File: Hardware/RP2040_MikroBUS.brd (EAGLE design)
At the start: 30.5 x 94 mm, 144 parts, among them J1 SWD, J3 Qwiic, J5 USB C, J6 microSD, Q1 20V/4.2A/52mΩ/1.4W, U2 MAX17048, U3 MCP73831, U4 W25QXX128MBIT, U5 RP2040, U6 WS2812-2020, U7 3.3V, Y2 12MHz

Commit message: Add raspi logos to repo
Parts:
- removed U$17: (no value), output:#I�C#0
- added U$72: (no value), output:#I2C#0
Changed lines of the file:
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@@
 <?xml version="1.0" encoding="utf-8"?>
 <!DOCTYPE eagle SYSTEM "eagle.dtd">
-<eagle version="9.5.2">
+<eagle version="9.4.2">
 <drawing>
 <settings>
-<setting alwaysvectorfont="no"/>
+<setting alwaysvectorfont="yes"/>
 <setting keepoldvectorfont="yes"/>
 <setting verticaltext="up"/>
@@
 <layer number="95" name="Names" color="7" fill="1" visible="no" active="no"/>
 <layer number="96" name="Values" color="7" fill="1" visible="no" active="no"/>
-<layer number="2" name="gndvert" color="10" fill="7" visible="yes" active="yes"/>
-<layer number="15" name="pwrhorz" color="4" fill="7" visible="yes" active="yes"/>
+<layer number="2" name="gndvert" color="10" fill="7" visible="no" active="yes"/>
+<layer number="15" name="pwrhorz" color="4" fill="7" visible="no" active="yes"/>
 <layer number="3" name="Route3" color="4" fill="3" visible="no" active="no"/>
 <layer number="4" name="Route4" color="1" fill="4" visible="no" active="no"/>
@@
 </polygon>
 <text x="13.081" y="-19.177" size="1.778" layer="51" font="vector" ratio="15">N. Poole</text>
-<polygon width="0.2032" layer="22">
-<vertex x="12.0396" y="11.2522"/>
-<vertex x="10.033" y="11.2522"/>
-<vertex x="10.033" y="10.5156"/>
-<vertex x="11.049" y="10.5156"/>
-<vertex x="11.049" y="11.2268"/>
-<vertex x="11.4046" y="11.2268"/>
-</polygon>
-<polygon width="0.2032" layer="22">
-<vertex x="11.811" y="7.7978"/>
-<vertex x="10.033" y="7.7978"/>
-<vertex x="10.033" y="8.5598"/>
-<vertex x="11.049" y="8.5598"/>
-<vertex x="11.049" y="7.7978"/>
-</polygon>
 <text x="48.26" y="45.72" size="1.778" layer="51" font="vector" ratio="15">Four Layer</text>
 <text x="48.26" y="43.18" size="1.778" layer="51" font="vector" ratio="15">1.6mm FR4</text>
@@
 </element>
 <element name="U$16" library="output" package="PWR0" value="" x="22.86" y="5.08" smashed="yes"/>
-<element name="U$17" library="output" package="#I�C#0" value="" x="10.4394" y="9.525" smashed="yes" rot="MR90"/>
 <element name="U$45" library="SparkFun-Aesthetics" package="SFE_LOGO_NAME_.1" value="" x="12.261" y="91.2506" smashed="yes"/>
 <element name="TP1" library="SparkFun-Connectors" package="PAD.03X.04" value="TEST-POINT3X4" x="6.35" y="30.48" smashed="yes" rot="MR0"/>
@@
 <element name="U$53" library="output" package="#_0#TX#0" value="" x="25.019" y="49.53" smashed="yes" rot="MR0"/>
 <element name="U$71" library="output" package="#_WS2812#0" value="" x="25.019" y="52.07" smashed="yes" rot="MR0"/>
+<element name="U$72" library="output" package="#I2C#0" value="" x="10.033" y="7.62" smashed="yes" rot="MR90"/>
 </elements>
 <signals>

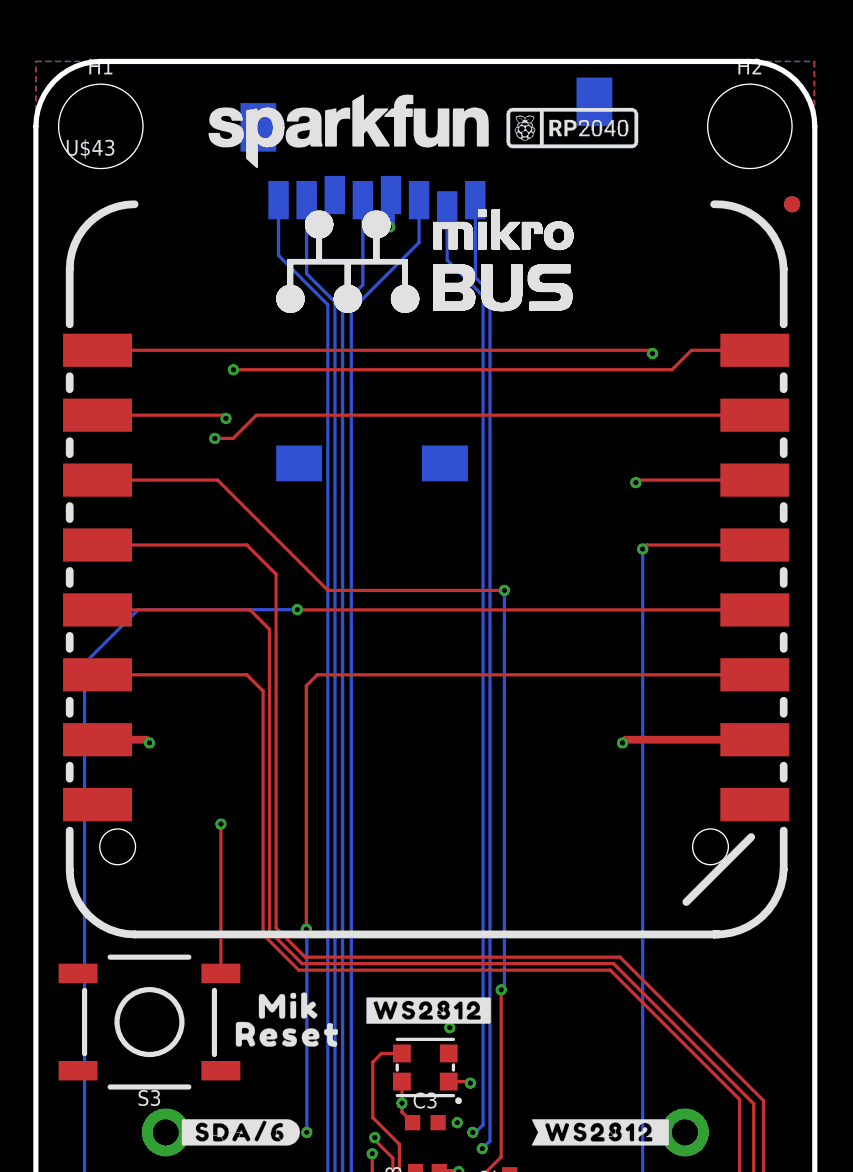
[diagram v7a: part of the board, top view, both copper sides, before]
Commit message: More of Pete's updates
* Fix I2C jumper label
* Update RP2040 logo and add to SF Eagle libraries
* Change "Mik" to "Mikro" for mikroBUS reset button
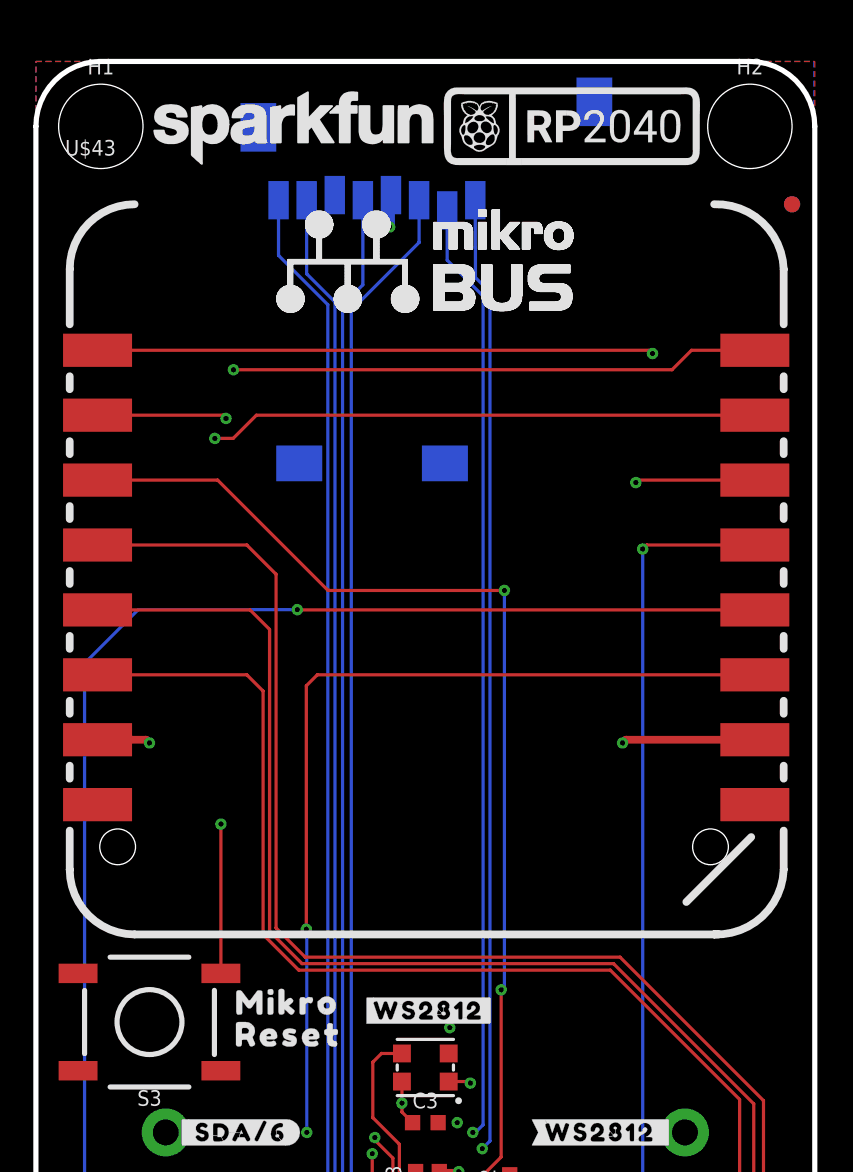
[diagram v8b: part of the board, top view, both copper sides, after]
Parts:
- removed U$30: (no value), RP2040:RP2040_20
- removed U$44: (no value), output:MIK0
- added U$17, U$73: RASPI_RP2040_LOGO_10MM, SparkFun-Aesthetics:RASPI_RP2040_LOGO_10MM
- U$29: device RP2040:RP2040_10 -> output:MIKRO0
- moved U$29 36.9 mm to (7.11, 57.1)
- moved U$45 2.16 mm to (10.1, 91.4)
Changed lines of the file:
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@@
 </element>
 <element name="U$16" library="output" package="PWR0" value="" x="22.86" y="5.08" smashed="yes"/>
-<element name="U$45" library="SparkFun-Aesthetics" package="SFE_LOGO_NAME_.1" value="" x="12.261" y="91.2506" smashed="yes"/>
+<element name="U$45" library="SparkFun-Aesthetics" package="SFE_LOGO_NAME_.1" value="" x="10.102" y="91.3776" smashed="yes"/>
 <element name="TP1" library="SparkFun-Connectors" package="PAD.03X.04" value="TEST-POINT3X4" x="6.35" y="30.48" smashed="yes" rot="MR0"/>
 <element name="TP2" library="SparkFun-Connectors" package="PAD.03X.04" value="TEST-POINT3X4" x="8.89" y="30.48" smashed="yes" rot="MR0"/>
 <element name="TP3" library="SparkFun-Connectors" package="PAD.03X.04" value="TEST-POINT3X4" x="11.43" y="30.48" smashed="yes" rot="MR0"/>
-<element name="U$30" library="RP2040" package="RP2040_20" value="" x="9.652" y="14.478" smashed="yes" rot="MR0"/>
-<element name="U$29" library="RP2040" package="RP2040_10" value="" x="20.993" y="91.374" smashed="yes"/>
 <element name="U$43" library="mikroBUS_SMD_BLACK" package="MIKROBUS_SMD_BLACK" package3d_urn="urn:adsk.eagle:package:18494266/4" value="MIKROBUS_SMD_BLACK1" x="15.113" y="73.787" smashed="yes">
 <attribute name="NAME" x="1.143" y="90.297" size="0.6096" layer="25" ratio="20"/>
@@
 <attribute name="VALUE" x="4.445" y="59.055" size="0.6096" layer="27" font="vector" ratio="20" rot="R180" align="top-center"/>
 </element>
-<element name="U$44" library="output" package="MIK0" value="" x="8" y="57" smashed="yes"/>
 <element name="U$46" library="output" package="RESET0" value="" x="7.1" y="55.9" smashed="yes"/>
 <element name="U$47" library="output" package="#_NC_#0" value="" x="22.098" y="36.83" smashed="yes"/>
@@
 <element name="U$71" library="output" package="#_WS2812#0" value="" x="25.019" y="52.07" smashed="yes" rot="MR0"/>
 <element name="U$72" library="output" package="#I2C#0" value="" x="10.033" y="7.62" smashed="yes" rot="MR90"/>
+<element name="U$17" library="SparkFun-Aesthetics" package="RASPI_RP2040_LOGO_10MM" value="RASPI_RP2040_LOGO_10MM" x="12.7" y="15.24" smashed="yes" rot="MR0"/>
+<element name="U$73" library="SparkFun-Aesthetics" package="RASPI_RP2040_LOGO_10MM" value="RASPI_RP2040_LOGO_10MM" x="20.955" y="91.44" smashed="yes"/>
+<element name="U$29" library="output" package="MIKRO0" value="" x="7.112" y="57.15" smashed="yes"/>
 </elements>
 <signals>
